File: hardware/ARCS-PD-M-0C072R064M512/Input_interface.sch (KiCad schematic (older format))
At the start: 78 parts

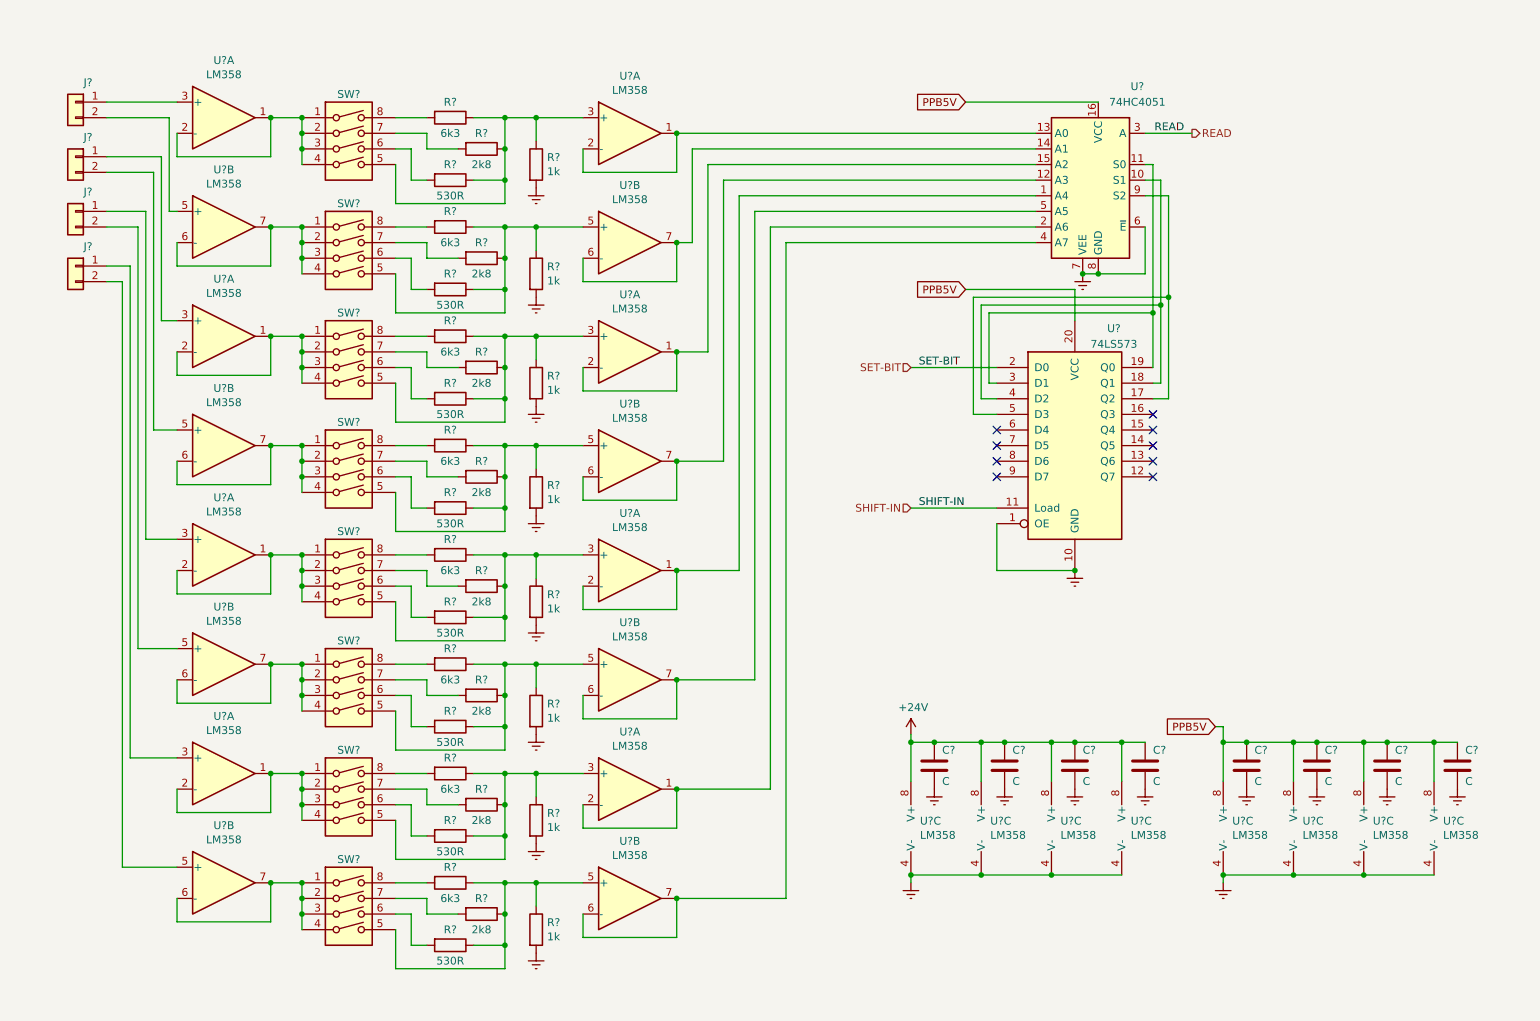
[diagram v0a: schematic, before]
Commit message: Create cards for input and output interface.
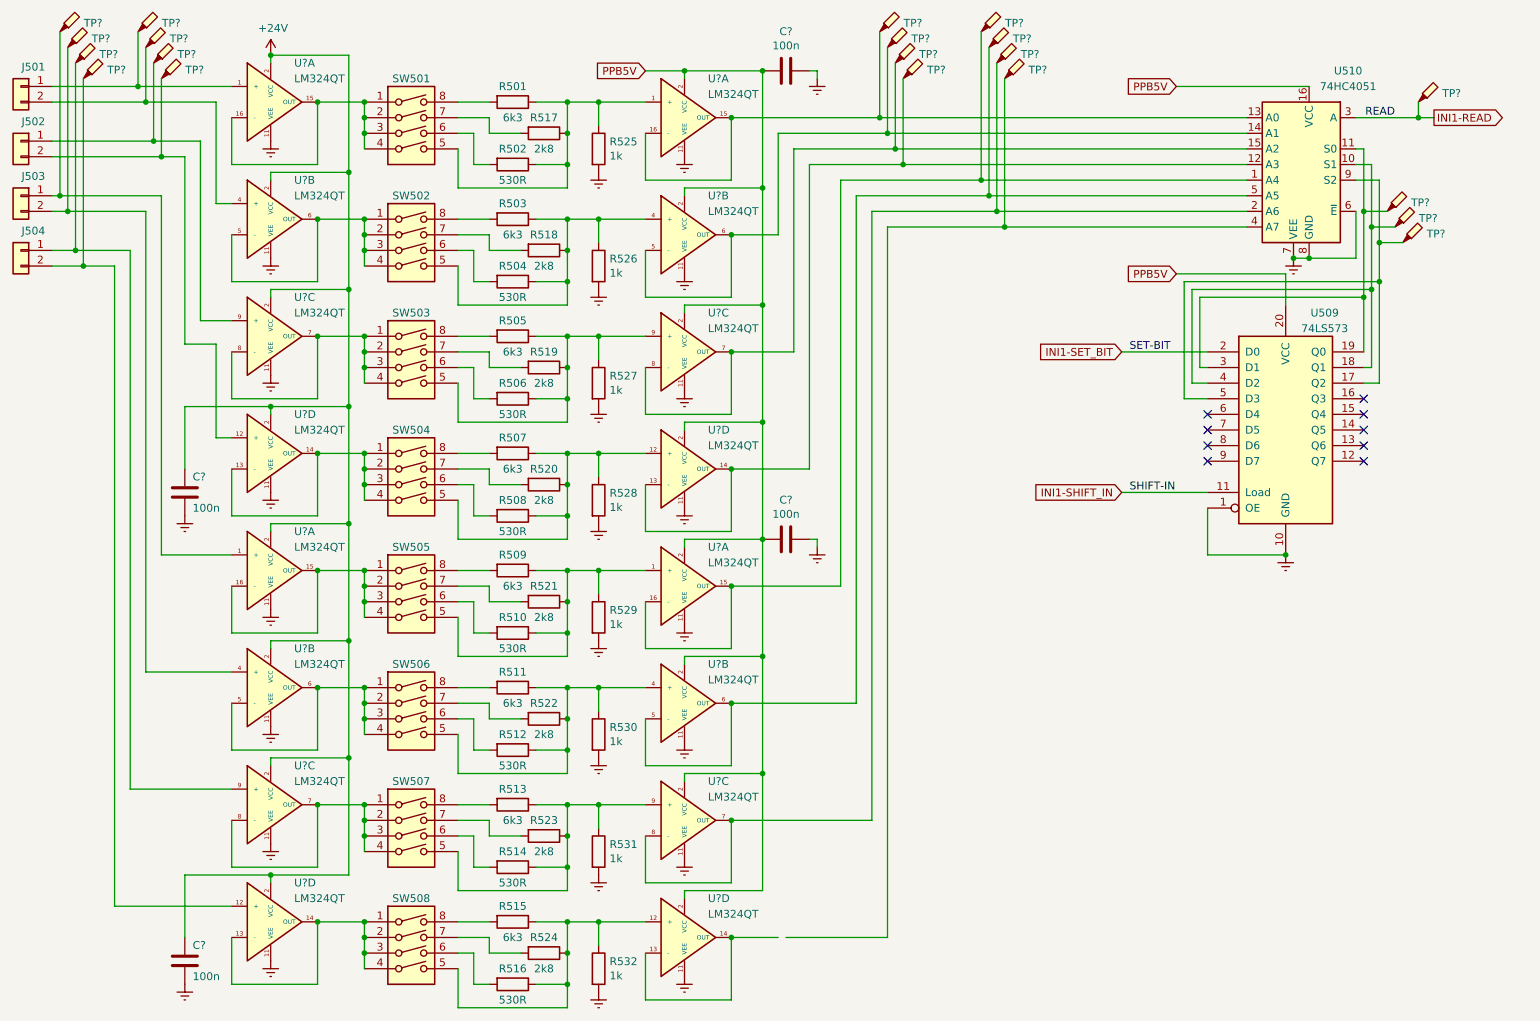
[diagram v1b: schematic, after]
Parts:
- removed C? (x8): C, symbol Device:C
- removed U? (x24): LM358, symbol Amplifier_Operational:LM358
- added C? (x4): 100n, symbol Device:C
- added TP? (x20): TestPoint_Probe, symbol Connector:TestPoint_Probe
- added U? (x16): LM324QT, symbol OPAmps:LM324QT
- gave numbers to parts that had none: 46
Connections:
- net +24V: now also C?.1, C?.1, U?.2 (VCC), U?.2 (VCC), U?.2 (VCC), U?.2 (VCC), U?.2 (VCC), U?.2 (VCC), U?.2 (VCC), U?.2 (VCC)
- net Earth: now also C?.1, C?.1, C?.2, C?.2, U?.11 (VEE), U?.11 (VEE), U?.11 (VEE), U?.11 (VEE), U?.11 (VEE), U?.11 (VEE), U?.11 (VEE), U?.11 (VEE), U?.11 (VEE), U?.11 (VEE), U?.11 (VEE), U?.11 (VEE), U?.11 (VEE), U?.11 (VEE), U?.11 (VEE), U?.11 (VEE)
- net PPB5V: now also C?.2, C?.2, U?.2 (VCC), U?.2 (VCC), U?.2 (VCC), U?.2 (VCC), U?.2 (VCC), U?.2 (VCC), U?.2 (VCC), U?.2 (VCC)
- net at SW501.1, SW501.2, SW501.3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: now also U?.15 (OUT), U?.16 (-)
- net at J501.1 (Pin_1): now also TP?.1, U?.1 (+)
- net at J501.2 (Pin_2): now also TP?.1, U?.4 (+)
- net at SW502.1, SW502.2, SW502.3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: now also U?.5 (-), U?.6 (OUT)
- net at J502.1 (Pin_1): now also TP?.1, U?.9 (+)
- net at J502.2 (Pin_2): now also TP?.1, U?.12 (+)
- net at J503.1 (Pin_1): now also TP?.1, U?.1 (+)
- net at J503.2 (Pin_2): now also TP?.1, U?.4 (+)
- net at J504.1 (Pin_1): now also TP?.1, U?.9 (+)
- net at J504.2 (Pin_2): now also TP?.1, U?.12 (+)
- net at SW503.1, SW503.2, SW503.3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: now also U?.7 (OUT), U?.8 (-)
- net at SW504.1, SW504.2, SW504.3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: now also U?.13 (-), U?.14 (OUT)
- net at SW505.1, SW505.2, SW505.3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: now also U?.15 (OUT), U?.16 (-)
- net at SW506.1, SW506.2, SW506.3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: now also U?.5 (-), U?.6 (OUT)
- net at SW507.1, SW507.2, SW507.3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: now also U?.7 (OUT), U?.8 (-)
- net at SW508.1, SW508.2, SW508.3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: now also U?.13 (-), U?.14 (OUT)
- net at R501.1, R502.1, R517.1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: now also U?.1 (+)
- net at U510.13 (A0): now also TP?.1, U?.15 (OUT), U?.16 (-)
- net at R503.1, R504.1, R518.1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: now also U?.4 (+)
- net at U510.14 (A1): now also TP?.1, U?.5 (-), U?.6 (OUT)
- net at U510.15 (A2): now also TP?.1, U?.7 (OUT), U?.8 (-)
- net at R505.1, R506.1, R519.1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: now also U?.9 (+)
- net at R507.1, R508.1, R520.1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: now also U?.12 (+)
- net at U510.12 (A3): now also TP?.1, U?.13 (-), U?.14 (OUT)
- net at U510.1 (A4): now also TP?.1, U?.15 (OUT), U?.16 (-)
- net at R509.1, R510.1, R521.1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: now also U?.1 (+)
- net at R511.1, R512.1, R522.1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: now also U?.4 (+)
- net at U510.5 (A5): now also TP?.1, U?.5 (-), U?.6 (OUT)
- net at U510.2 (A6): now also TP?.1, U?.7 (OUT), U?.8 (-)
- net at R513.1, R514.1, R523.1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: now also U?.9 (+)
- net at R515.1, R516.1, R524.1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: now also U?.12 (+)
- net at U510.4 (A7): now also TP?.1
- net at U509.18 (Q1), U509.4 (D2), U510.10 (S1): now also TP?.1
- net at U509.19 (Q0), U509.3 (D1), U510.11 (S0): now also TP?.1
- net at U509.17 (Q2), U509.5 (D3), U510.9 (S2): now also TP?.1
- net READ renamed INI1-READ
- net INI1-READ: now also TP?.1
- net SET-BIT renamed INI1-SET_BIT
- net SHIFT-IN renamed INI1-SHIFT_IN
- new net: U?.13 (-), U?.14 (OUT)
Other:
- moved on the sheet: J501, J502, J503, J504, R501, R502, R503, R504, R505, R506, R507, R508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
